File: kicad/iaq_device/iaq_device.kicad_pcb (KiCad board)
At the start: 2 copper layers, 70.1 x 43.2 mm, 19 parts, among them J1 External Pins, SW1 B3S-1000, SW2 CO2 CAL, U1 WeMos_D1_mini, U2 PMS7003, U3 SSD1306, U4 BME280, U5 MH-Z19, U6 SGP30, U7 TSL2561T

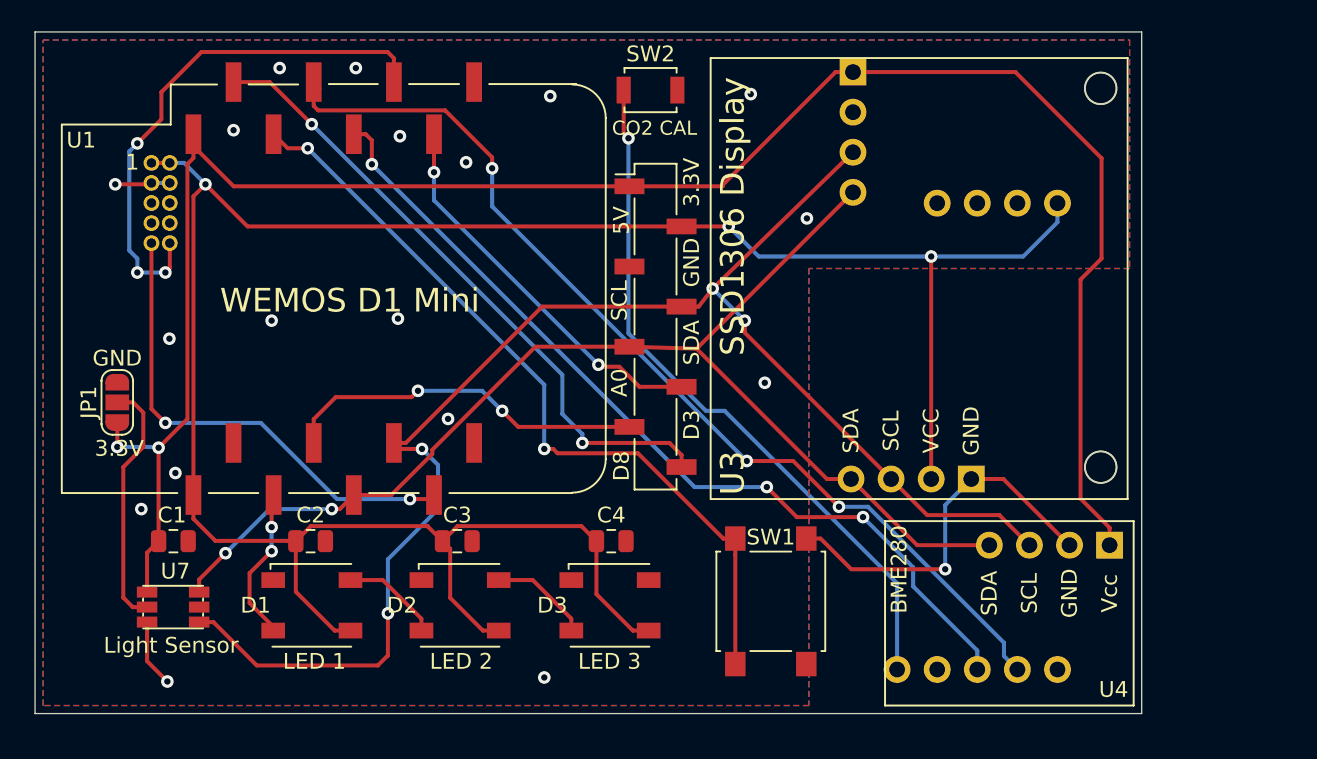
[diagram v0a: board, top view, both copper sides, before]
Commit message: fix stuff for kicad and adds scd30 co2 sensor symbol, footprint and 3d model
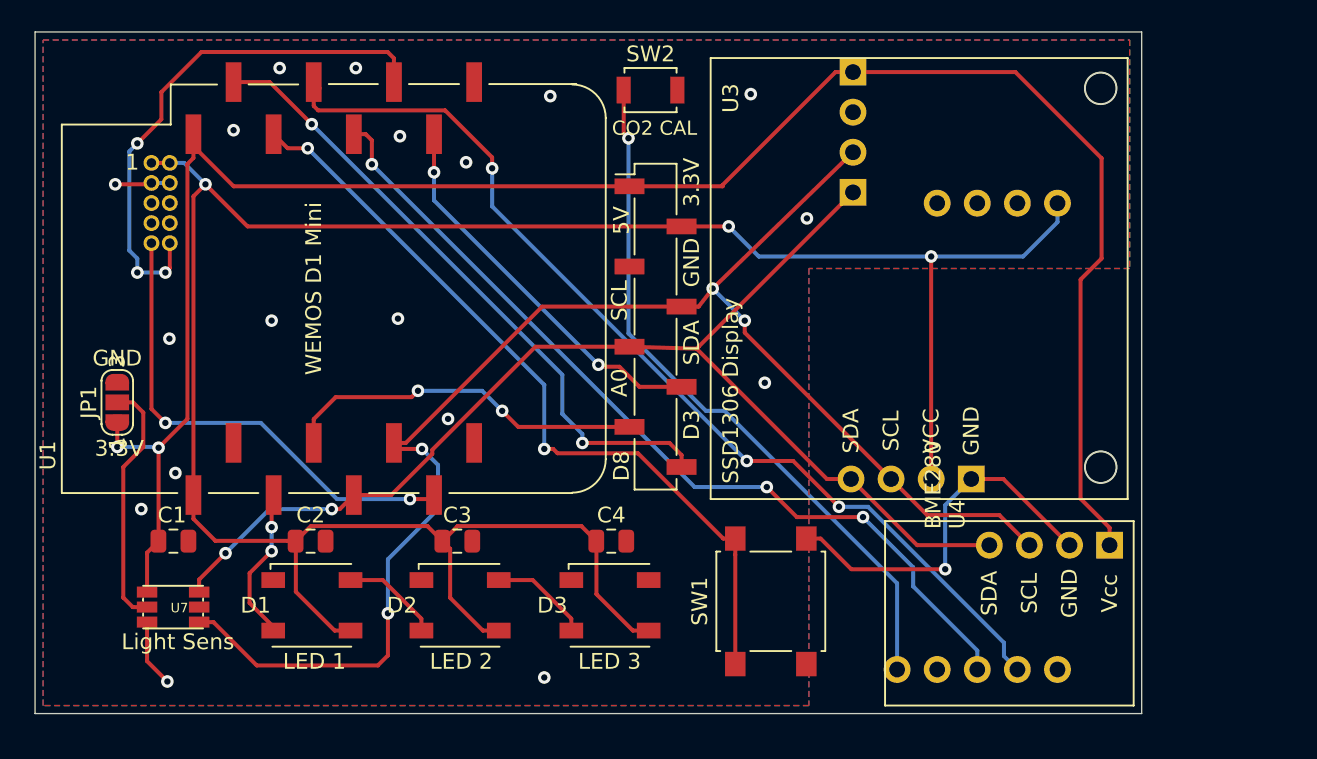
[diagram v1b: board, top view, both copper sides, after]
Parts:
- SW1: footprint Nikolay Library:SW_SPST_B3S-1000 -> iaq_board:SW_SPST_B3S-1000
- U1: value WeMos_D1_mini -> WeMos_D1_mini_ESP32; footprint Nikolay Library:WEMOS_D1_surface -> iaq_board:WEMOS_D1_surface
- U2: footprint Nikolay Library:PMS7003 -> iaq_board:PMS7003
- U3: footprint Nikolay Library:SSD1306 -> iaq_board:SSD1306
- U4: footprint Nikolay Library:BME280_breakout_6pin -> iaq_board:BME280_breakout_6pin
- U5: footprint Nikolay Library:MH-Z19 -> iaq_board:MH-Z19
- U6: footprint Nikolay Library:SGP30_breakout_4pin -> iaq_board:SGP30_breakout_4pin
- U7: footprint Nikolay Library:TSL2561T -> iaq_board:TSL2561T
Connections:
- D3 pad 4: (no net) -> unconnected-(D3-Pad4)
- U1 pad 1: (no net) -> unconnected-(U1-Pad1)
- U1 pad 16: (no net) -> unconnected-(U1-Pad16)
- U2 pad 5: (no net) -> unconnected-(U2-Pad5)
- U2 pad 6: (no net) -> unconnected-(U2-Pad6)
- U2 pad 7: (no net) -> unconnected-(U2-Pad7)
- U2 pad 8: (no net) -> unconnected-(U2-Pad8)
- U5 pad 1: (no net) -> unconnected-(U5-Pad1)
- U5 pad 4: (no net) -> unconnected-(U5-Pad4)
- U5 pad 8: (no net) -> unconnected-(U5-Pad8)
- U5 pad 9: (no net) -> unconnected-(U5-Pad9)
- U7 pad 5: (no net) -> unconnected-(U7-Pad5)
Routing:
- net GND: track 31.8 -> 76.3 mm, vias 19 -> 20
- net Net-(SW2-Pad2): track 44.6 -> 0.00 mm, vias 1 -> 0
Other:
- net class Default removed

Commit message: lots of changes
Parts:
- removed ?: , 
- removed SW2: CO2 CAL, Button_Switch_SMD:SW_SPST_B3U-1000P
- U1: footprint iaq_board:WEMOS_D1_surface -> Module:WEMOS_D1_mini_light
- U5: value MH-Z19 -> SCD30; footprint iaq_board:MH-Z19 -> iaq_board:SCD30
- moved U5 15.9 mm to (164.4, 98.4)
- moved U4 5.65 mm to (152.8, 106.8)
- moved U3 1.38 mm to (159.5, 102.2)
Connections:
- net Net-(SW1-Pad1) renamed /SEL_BTN
- C1 pad 1: +3V3 -> +3.3V
- J1 pad 1: +3V3 -> +3.3V
- JP1 pad 1: +3V3 -> +3.3V
- U1 pad 4: MH_RX -> unconnected-(U1-SCK/D5-Pad4)
- U1 pad 5: MH_TX -> unconnected-(U1-MISO/D6-Pad5)
- U1 pad 8: +3V3 -> +3.3V
- U4 pad 1: +3V3 -> +3.3V
- U5 pad 1: unconnected-(U5-Pad1) -> +3.3V
- U5 pad 2: MH_TX -> GND
- U5 pad 3: MH_RX -> SCL
- U5 pad 4: unconnected-(U5-Pad4) -> SDA
- U5 pad 5: Net-(SW2-Pad2) -> unconnected-(U5-RDY-Pad5)
- U5 pad 6: +5V -> unconnected-(U5-PWM-Pad6)
- U6 pad 1: +3V3 -> +3.3V
- U7 pad 1: +3V3 -> +3.3V
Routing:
- net +3.3V: track 0.00 -> 154.9 mm, vias 0 -> 2
- net +3V3: track 124.9 -> 0.00 mm, vias 2 -> 0
- net GND: track 76.3 -> 7.81 mm, vias 20 -> 18
- net MH_TX: track 63.7 -> 0.00 mm, vias 3 -> 0
- net MH_RX: track 56.1 -> 0.00 mm, vias 3 -> 0
- net SDA: track 76.3 -> 114.3 mm
- net SCL: track 94.1 -> 114.8 mm, vias 4 -> 1
- net +5V: track 148.3 -> 133.2 mm, vias 3 -> 2
- net PMS_RX: track 30.9 -> 24.4 mm, vias 2 -> 0
- net A0: track 24.8 -> 28.5 mm, vias 2 -> 1
- net PMS_SET: track 33.7 -> 37.3 mm, vias 3 -> 0
- net LED_D: track 10.2 -> 11.8 mm
- net /SEL_BTN: track 50.2 -> 49.0 mm, vias 2 -> 1
- net D3: track 23.2 -> 22.5 mm, vias 2 -> 0
- net D8: track 40.7 -> 40.8 mm, vias 2 -> 1
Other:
- board size 70.1 x 43.2 mm -> 79 x 43 mm
- board text added: "https://github.com/koekie/iaq_board"
- board text removed: "CO2 CAL"
- board text removed: "https://github.com/nkitanov/iaq_board"

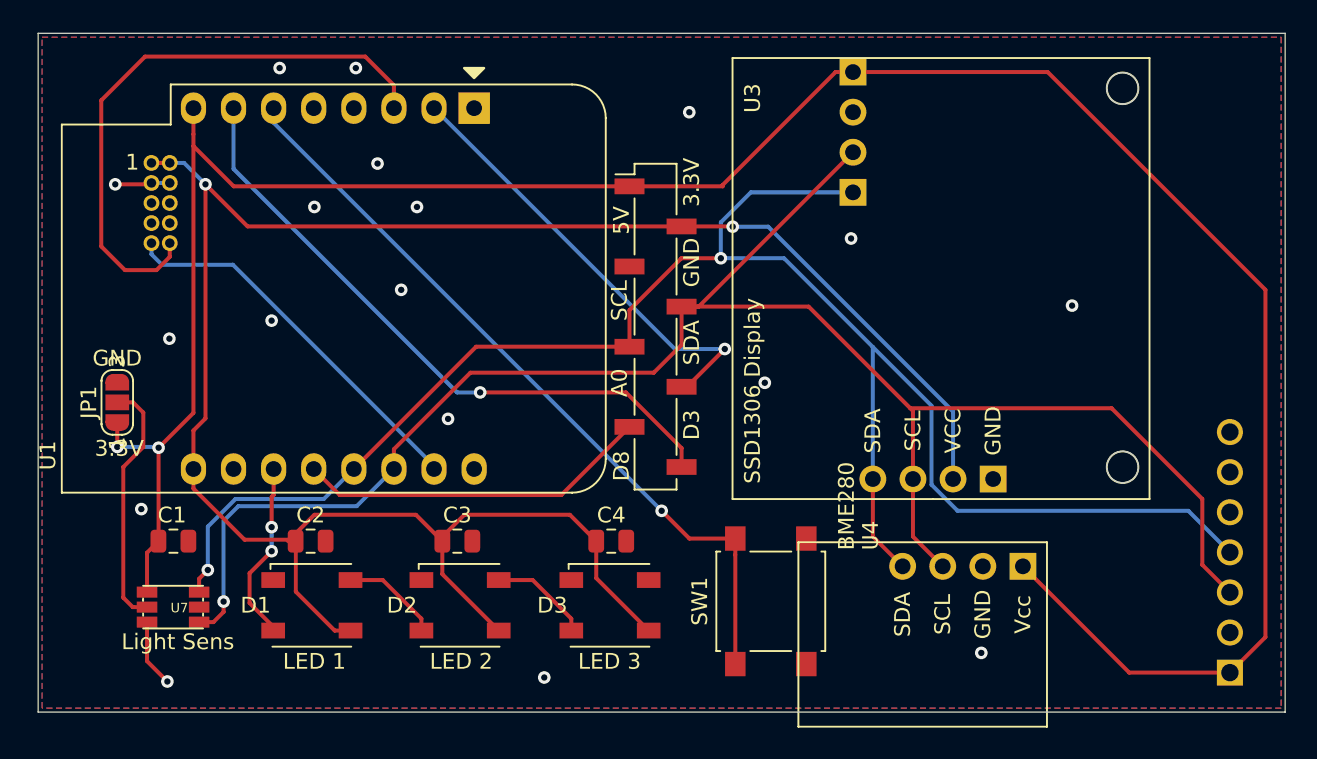
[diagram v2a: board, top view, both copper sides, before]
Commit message: changed co2 sensor to scd30 and rerouted the board
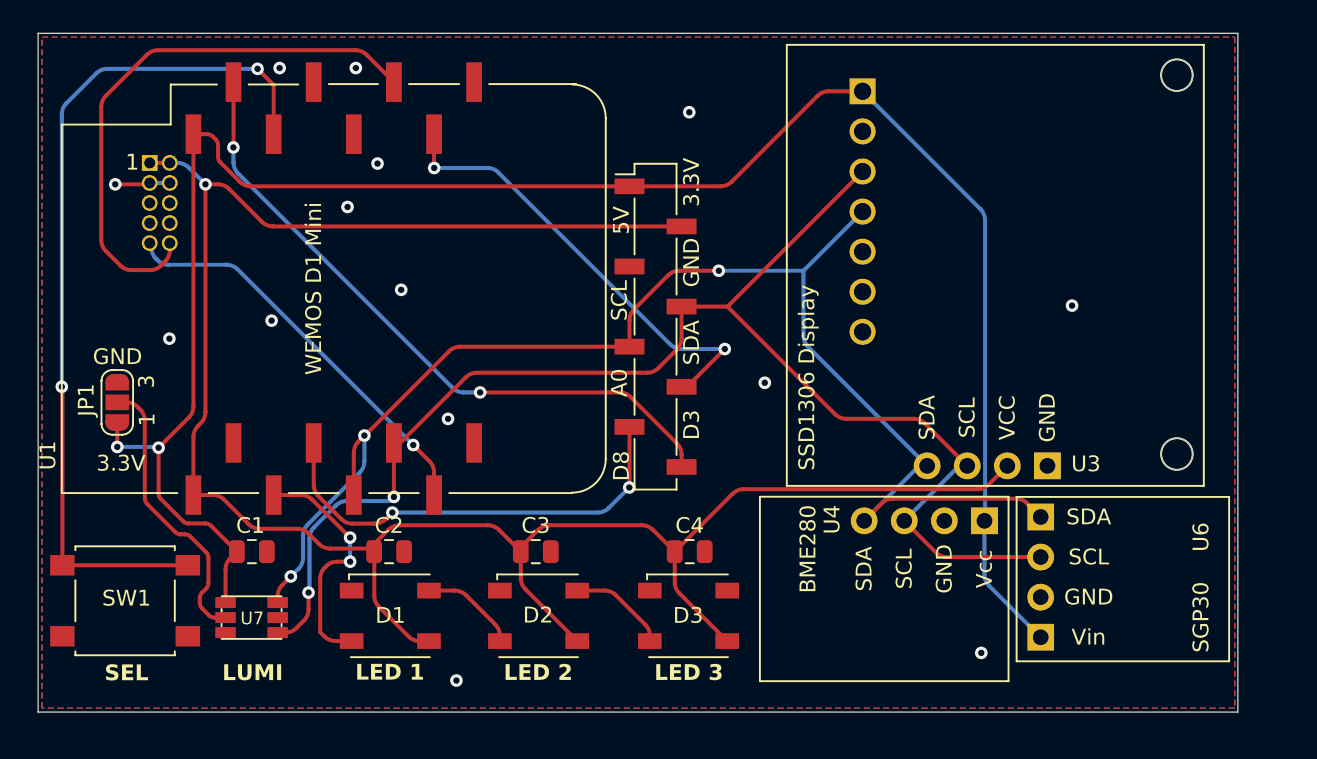
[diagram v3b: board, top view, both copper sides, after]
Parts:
- U1: footprint Module:WEMOS_D1_mini_light -> iaq_board:WEMOS_D1_surface
- U6: moved to F.Cu
- moved SW1 40.9 mm to (104.5, 110.0), turned to 0 degrees
- moved U6 37.7 mm to (162.5, 112.3)
- moved U5 5.55 mm to (161.3, 93.8), turned to -90 degrees
- moved C2 5.02 mm to (121.2, 106.8)
- moved C4 5.02 mm to (140.3, 106.8)
- moved C1 5.02 mm to (112.5, 106.8)
- moved C3 5.02 mm to (130.5, 106.8)
- moved D1 5.02 mm to (121.3, 110.9)
- moved D2 5.02 mm to (130.7, 110.9)
- moved U7 5.02 mm to (110.9, 110.1)
- moved D3 5.02 mm to (140.2, 110.9)
- moved U4 3.78 mm to (150.3, 103.9)
- moved U3 3.54 mm to (162.9, 101.4)
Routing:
- net +3.3V: track 154.9 -> 123.0 mm
- net SDA: track 114.3 -> 88.3 mm, vias 2 -> 3
- net SCL: track 114.8 -> 89.3 mm, vias 1 -> 2
- net D3: track 22.5 -> 28.5 mm, vias 0 -> 2
- net /SEL_BTN: track 49.0 -> 54.8 mm, vias 1 -> 2
- net GND: track 7.81 -> 3.52 mm, vias 18 -> 14
- net LED_D: track 11.8 -> 15.5 mm
- net Net-(JP1-C): track 15.9 -> 18.2 mm
- net +5V: track 133.2 -> 134.7 mm, vias 2 -> 1
- net PMS_SET: track 37.3 -> 35.8 mm
- net D8: track 40.8 -> 42.2 mm, vias 1 -> 2
- net PMS_RX: track 24.4 -> 25.4 mm, vias 0 -> 1
- net A0: track 28.5 -> 28.9 mm, vias 1 -> 2
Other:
- board size 79 x 43 mm -> 76 x 43 mm
- rule pad_to_mask_clearance: 0.051 -> 0
- board text added: "JLCJLCJLCJLC"
- board text added: "Wemos D1 Mini Air Quality Board rev.2.0"
- board text removed: "Wemos D1 Mini Air Quality Board rev.1.1"
